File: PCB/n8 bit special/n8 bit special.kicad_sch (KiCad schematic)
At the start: 45 parts, among them J1 USB_B_Micro, J2 PORT0, J3 PORT1, J4 PORT2, J6 Conn_02x08_Odd_Even, Q1 2N3904, SW1 SW_Push_Dual, U1 W65C02SxP, U10 74HC00, U2 CY62256-70PC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

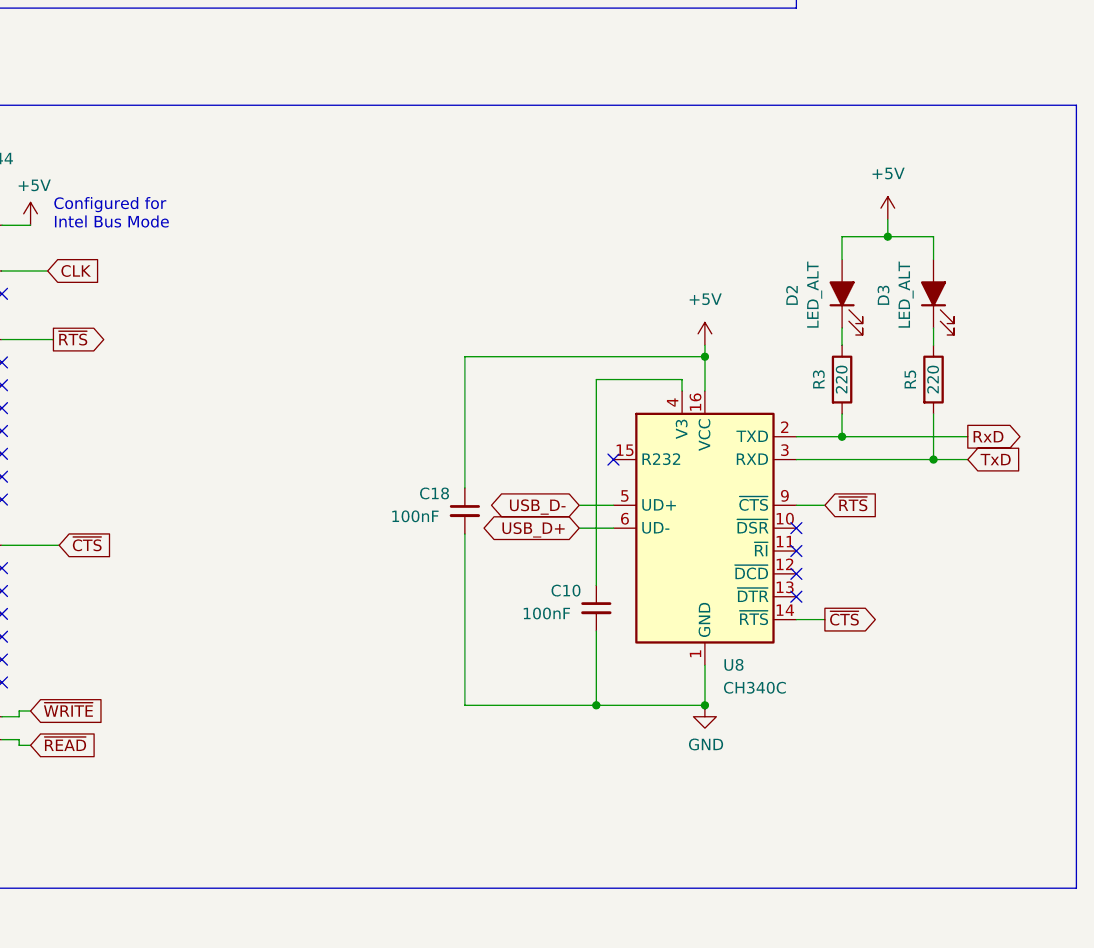
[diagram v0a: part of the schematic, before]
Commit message: Pre-import stage of autorouting
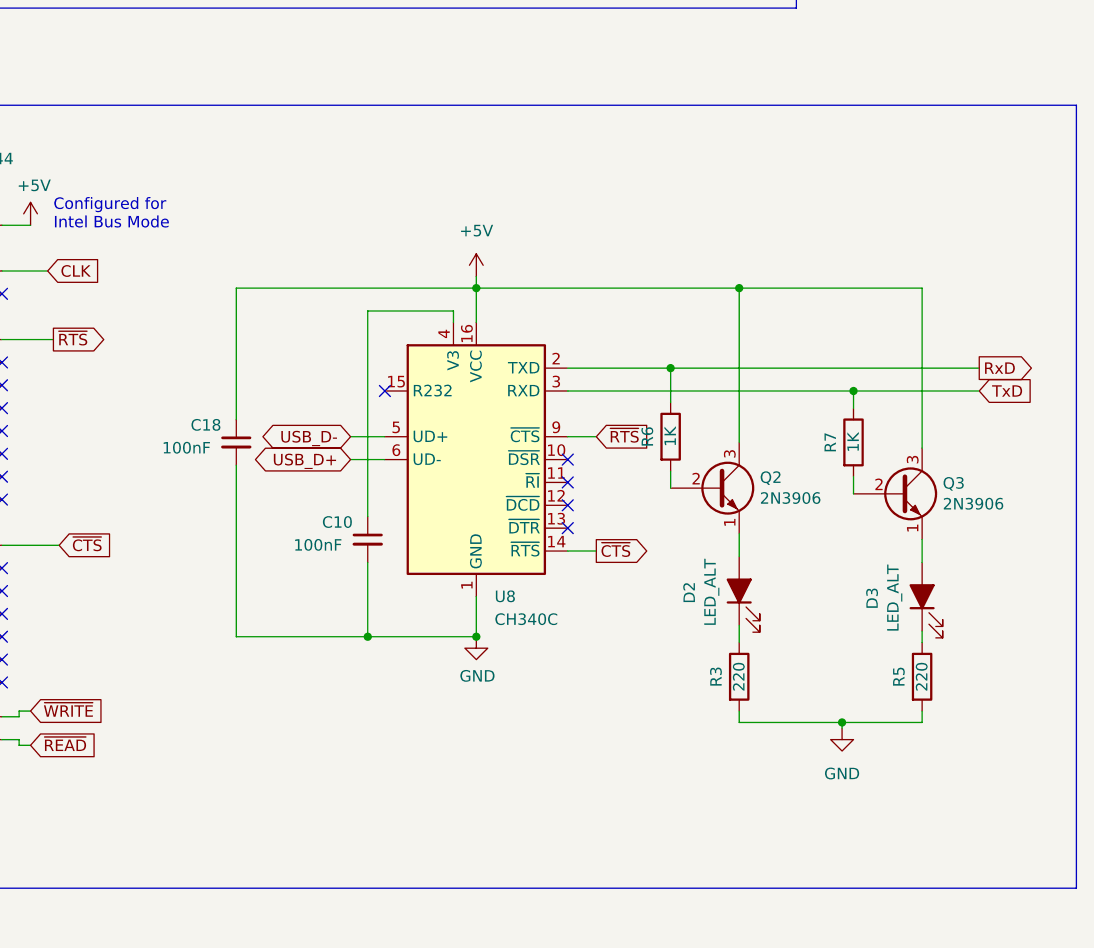
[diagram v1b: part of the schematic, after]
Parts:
- added Q2, Q3: 2N3906, Package_TO_SOT_THT:TO-92, symbol Transistor_BJT:2N3904
- added R6, R7: 1K, Resistor_THT:R_Axial_DIN0207_L6.3mm_D2.5mm_P7.62mm_Horizontal, symbol Device:R
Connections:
- net +5V: now also Q2.3 (C), Q3.3 (C); no longer D2.2 (A), D3.2 (A)
- net GND: now also R3.2, R5.2
- net RxD: now also R6.1; no longer R3.2
- net TxD: now also R7.1; no longer R5.2
- new net: D3.2 (A), Q3.1 (E)
- new net: Q3.2 (B), R7.2
- new net: D2.2 (A), Q2.1 (E)
- new net: Q2.2 (B), R6.2
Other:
- moved on the sheet: C10, C18, D2, D3, R3, R5, U8
